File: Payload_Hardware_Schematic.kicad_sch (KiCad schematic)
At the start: 8 parts, among them J1 Micro_SD_Card, J2 Conn_01x02_Socket, J4 Conn_01x02, U1 STM32F411 BlackPill, U2 MPM3610, U4 LSM9DS1, U5 MPM3610, U6 BMP388

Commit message: servo pins
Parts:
- added J3, J5: Conn_01x04_Pin, Connector_PinHeader_2.54mm:PinHeader_1x04_P2.54mm_Vertical, symbol Connector:Conn_01x04_Pin
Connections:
- net 5V: now also J3.3 (Pin_3), J5.3 (Pin_3)
- net FDBK1: now also J3.1 (Pin_1)
- net GND: now also J3.4 (Pin_4), J5.4 (Pin_4)
- net TIM1: now also J3.2 (Pin_2)
- net TIM2: now also J5.2 (Pin_2)
- net FDBK renamed FDBK2
- net FDBK2: now also J5.1 (Pin_1)
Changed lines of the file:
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@@
+		)
+	)
+	(label "GND"
+		(at 121.92 100.33 0)
+		(effects
+			(font
+				(size 1.27 1.27)
+				(thickness 0.254)
+				(bold yes)
+			)
+			(justify left bottom)
 		)
 	)
@@
 		)
 	)
+	(label "5V"
+		(at 140.97 97.79 0)
+		(effects
+			(font
+				(size 1.27 1.27)
+				(thickness 0.254)
+				(bold yes)
+				(color 255 0 0 1)
+			)
+			(justify left bottom)
+		)
+	)
+	(label "5V"
+		(at 121.92 97.79 0)
+		(effects
+			(font
+				(size 1.27 1.27)
+				(thickness 0.254)
+				(bold yes)
+				(color 255 0 0 1)
+			)
+			(justify left bottom)
+		)
+	)
 	(label "MISO4"
 		(at 29.21 39.37 180)
@@
 				(thickness 0.254)
 				(bold yes)
-				(color 23 39 255 1)
+				(color 70 255 55 1)
 			)
 			(justify left bottom)
@@
 		)
 	)
-	(label "FDBK"
+	(label "FDBK2"
 		(at 242.57 34.29 0)
 		(effects
@@
 				(thickness 0.254)
 				(bold yes)
-				(color 164 74 255 1)
+				(color 0 255 0 1)
 			)
 			(justify left bottom)
@@
 		)
 	)
+	(label "GND"
+		(at 140.97 100.33 0)
+		(effects
+			(font
+				(size 1.27 1.27)
+				(thickness 0.254)
+				(bold yes)
+			)
+			(justify left bottom)
+		)
+	)
 	(label "SCK3"
 		(at 157.48 38.1 0)
@@
 		)
 	)
+	(label "FDBK2"
+		(at 121.92 92.71 0)
+		(effects
+			(font
+				(size 1.27 1.27)
+				(thickness 0.254)
+				(bold yes)
+				(color 0 255 0 1)
+			)
+			(justify left bottom)
+		)
+	)
 	(label "MISO3"
 		(at 157.48 35.56 0)
@@
 		)
 	)
+	(label "TIM2"
+		(at 121.92 95.25 0)
+		(effects
+			(font
+				(size 1.27 1.27)
+			)
+			(justify left bottom)
+		)
+	)
 	(label "SCK2"
 		(at 83.82 36.83 180)
@@
 		)
 	)
+	(label "FDBK1"
+		(at 140.97 92.71 0)
+		(effects
+			(font
+				(size 1.27 1.27)
+				(thickness 0.254)
+				(bold yes)
+				(color 70 255 55 1)
+			)
+			(justify left bottom)
+		)
+	)
 	(label "MOSI4"
 		(at 186.69 41.91 180)
@@
 				(bold yes)
 				(color 23 39 255 1)
+			)
+			(justify left bottom)
+		)
+	)
+	(label "TIM1"
+		(at 140.97 95.25 0)
+		(effects
+			(font
+				(size 1.27 1.27)
 			)
 			(justify left bottom)
@@
 		(on_board yes)
 		(dnp no)
-		(fields_autoplaced yes)
 		(property "Reference" "U5"
 			(at 148.59 67.31 0)
@@
 	)
 	(symbol
+		(lib_id "Connector:Conn_01x04_Pin")
+		(at 135.89 95.25 0)
+		(unit 1)
+		(exclude_from_sim no)
+		(in_bom yes)
+		(on_board yes)
+		(dnp no)
+		(fields_autoplaced yes)
+		(property "Reference" "J3"
+			(at 136.525 87.63 0)
+			(effects
+				(font
+					(size 1.27 1.27)
+				)
+			)
+		)
+		(property "Value" "Conn_01x04_Pin"
+			(at 136.525 90.17 0)
+			(effects
+				(font
+					(size 1.27 1.27)
+				)
+			)
+		)
+		(property "Footprint" "Connector_PinHeader_2.54mm:PinHeader_1x04_P2.54mm_Vertical"
+			(at 135.89 95.25 0)
+			(effects
+				(font
+					(size 1.27 1.27)
+				)
+				(hide yes)
+			)
+		)
+		(property "Datasheet" "~"
+			(at 135.89 95.25 0)
+			(effects
+				(font
+					(size 1.27 1.27)
+				)
+				(hide yes)
+			)
+		)
+		(property "Description" "Generic connector, single row, 01x04, script generated"
+			(at 135.89 95.25 0)
+			(effects
+				(font
+					(size 1.27 1.27)
+				)
+				(hide yes)
+			)
+		)
+		(pin "2"
+		)
+		(pin "1"
+		)
+		(pin "4"
+		)
+		(pin "3"
+		)
+		(instances
+			(project ""
+				(path "/f4ead8bb-2437-4e54-a6d9-f5ca11bfd675"
+					(reference "J3")
+					(unit 1)
+				)
+			)
+		)
+	)
+	(symbol
 		(lib_id "Payload-STM32:STM32F411_Black_Pill")
 		(at 214.63 53.34 0)
@@
 					(unit 1)
 				)
+			)
+		)
+	)
+	(symbol
+		(lib_id "Connector:Conn_01x04_Pin")
+		(at 116.84 95.25 0)
+		(unit 1)
+		(exclude_from_sim no)
+		(in_bom yes)
+		(on_board yes)
+		(dnp no)
+		(property "Reference" "J5"
+			(at 117.475 87.63 0)
+			(effects
+				(font
+					(size 1.27 1.27)
+				)
+			)
+		)
+		(property "Value" "Conn_01x04_Pin"
+			(at 117.475 90.17 0)
+			(effects
+				(font
+					(size 1.27 1.27)
+				)
+			)
+		)
+		(property "Footprint" "Connector_PinHeader_2.54mm:PinHeader_1x04_P2.54mm_Vertical"
+			(at 116.84 95.25 0)
+			(effects
+				(font
+					(size 1.27 1.27)
+				)
+				(hide yes)
+			)
+		)
+		(property "Datasheet" "~"
+			(at 116.84 95.25 0)
+			(effects
+				(font
+					(size 1.27 1.27)
+				)
+				(hide yes)
+			)
+		)
+		(property "Description" "Generic connector, single row, 01x04, script generated"
+			(at 116.84 95.25 0)
+			(effects
+				(font
+					(size 1.27 1.27)
+				)
+				(hide yes)
+			)
+		)
+		(pin "2"
+		)
+		(pin "1"
+		)
+		(pin "4"
+		)
+		(pin "3"
+		)
+		(instances
+			(project "Payload_Hardware_Schematic"
+				(path "/f4ead8bb-2437-4e54-a6d9-f5ca11bfd675"
+					(reference "J5")
+					(unit 1)
+				)

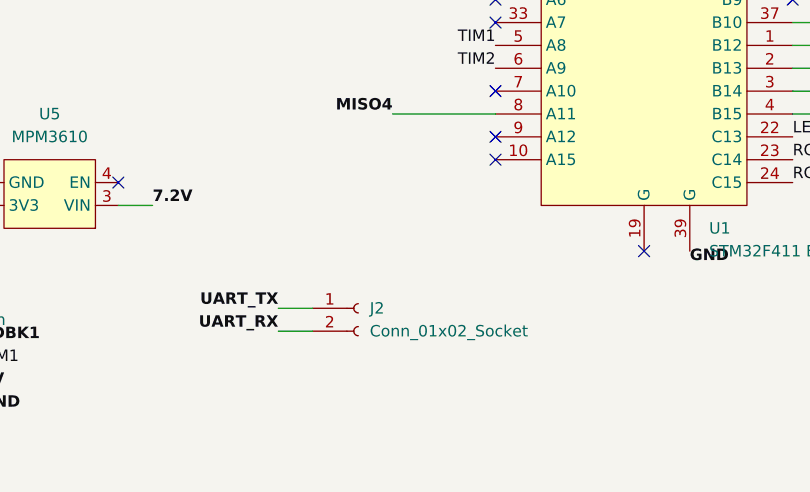
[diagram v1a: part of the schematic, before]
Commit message: added DIO SCK
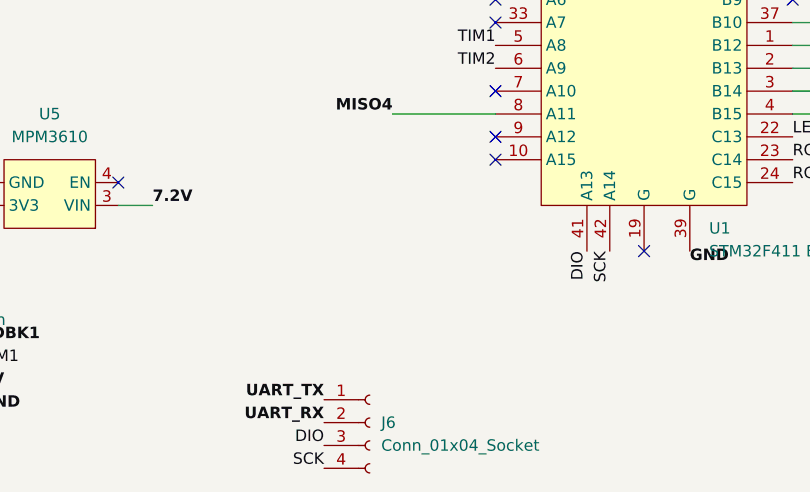
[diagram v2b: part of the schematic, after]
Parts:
- removed J2: Conn_01x02_Socket, Connector_PinSocket_2.54mm:PinSocket_1x02_P2.54mm_Vertical, symbol Connector:Conn_01x02_Socket
- added J6: Conn_01x04_Socket, symbol Connector:Conn_01x04_Socket
- U1: footprint Avionics_Symbols:STM32F411 -> Payload-STM32:STM32F411_Black_Pill
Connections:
- net UART_RX: now also J6.2 (Pin_2)
- net UART_TX: now also J6.1 (Pin_1)
- new net DIO: J6.3 (Pin_3), U1.41 (A13)
- new net SCK: J6.4 (Pin_4), U1.42 (A14)
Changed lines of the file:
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@@
-	(wire
-		(pts
-			(xy 173.99 88.9) (xy 177.8 88.9)
-		)
-		(stroke
-			(width 0)
-			(type default)
-		)
-	)
 	(wire
 		(pts
@@
 		(pts
 			(xy 83.82 41.91) (xy 88.9 41.91)
-		)
-		(stroke
-			(width 0)
-			(type default)
-		)
-	)
-	(wire
-		(pts
-			(xy 173.99 91.44) (xy 177.8 91.44)
 		)
 		(stroke
@@
 		)
 	)
+	(label "DIO"
+		(at 208.28 82.55 270)
+		(effects
+			(font
+				(size 1.27 1.27)
+			)
+			(justify right bottom)
+		)
+	)
 	(label "CSIMU"
 		(at 231.14 46.99 0)
@@
 		)
 	)
+	(label "SCK"
+		(at 210.82 82.55 270)
+		(effects
+			(font
+				(size 1.27 1.27)
+			)
+			(justify right bottom)
+		)
+	)
 	(label "GND"
 		(at 140.97 100.33 0)
@@
 		)
 	)
+	(label "UART_RX"
+		(at 179.07 101.6 180)
+		(effects
+			(font
+				(size 1.27 1.27)
+				(thickness 0.254)
+				(bold yes)
+				(color 221 133 0 1)
+			)
+			(justify right bottom)
+		)
+	)
 	(label "3.3V"
 		(at 215.9 20.32 0)
@@
 		)
 	)
+	(label "SCK"
+		(at 179.07 106.68 180)
+		(effects
+			(font
+				(size 1.27 1.27)
+			)
+			(justify right bottom)
+		)
+	)
 	(label "RCC_OSC32_OUT"
 		(at 231.14 74.93 0)
@@
 		)
 	)
+	(label "DIO"
+		(at 179.07 104.14 180)
+		(effects
+			(font
+				(size 1.27 1.27)
+			)
+			(justify right bottom)
+		)
+	)
 	(label "GND"
 		(at 58.42 74.93 180)
@@
 		)
 	)
-	(label "UART_RX"
-		(at 173.99 91.44 180)
-		(effects
-			(font
-				(size 1.27 1.27)
-				(thickness 0.254)
-				(bold yes)
-				(color 221 133 0 1)
-			)
-			(justify right bottom)
-		)
-	)
 	(label "BTN"
 		(at 198.12 39.37 180)
@@
 	)
 	(label "UART_TX"
-		(at 173.99 88.9 180)
+		(at 179.07 99.06 180)
 		(effects
 			(font
@@
 	)
 	(symbol
+		(lib_id "Connector:Conn_01x04_Socket")
+		(at 184.15 101.6 0)
+		(unit 1)
+		(exclude_from_sim no)
+		(in_bom yes)
+		(on_board yes)
+		(dnp no)
+		(fields_autoplaced yes)
+		(property "Reference" "J6"
+			(at 185.42 101.5999 0)
+			(effects
+				(font
+					(size 1.27 1.27)
+				)
+				(justify left)
+			)
+		)
+		(property "Value" "Conn_01x04_Socket"
+			(at 185.42 104.1399 0)
+			(effects
+				(font
+					(size 1.27 1.27)
+				)
+				(justify left)
+			)
+		)
+		(property "Footprint" ""
+			(at 184.15 101.6 0)
+			(effects
+				(font
+					(size 1.27 1.27)
+				)
+				(hide yes)
+			)
+		)
+		(property "Datasheet" "~"
+			(at 184.15 101.6 0)
+			(effects
+				(font
+					(size 1.27 1.27)
+				)
+				(hide yes)
+			)
+		)
+		(property "Description" "Generic connector, single row, 01x04, script generated"
+			(at 184.15 101.6 0)
+			(effects
+				(font
+					(size 1.27 1.27)
+				)
+				(hide yes)
+			)
+		)
+		(pin "4"
+		)
+		(pin "2"
+		)
+		(pin "1"
+		)
+		(pin "3"
+		)
+		(instances
+			(project ""
+				(path "/f4ead8bb-2437-4e54-a6d9-f5ca11bfd675"
+					(reference "J6")
+					(unit 1)
+				)
+			)
+		)
+	)
+	(symbol
 		(lib_id "Connector:Conn_01x04_Pin")
 		(at 135.89 95.25 0)
@@
 			)
 		)
-		(property "Footprint" "Avionics_Symbols:STM32F411"
+		(property "Footprint" "Payload-STM32:STM32F411_Black_Pill"
 			(at 210.82 39.37 0)
 			(effects
@@
 		)
 		(pin "24"
+		)
+		(pin "42"
+		)
+		(pin "41"
 		)
 		(instances
@@
 					(unit 1)
 				)
-			)
-		)
-	)
-	(symbol
-		(lib_id "Connector:Conn_01x02_Socket")
-		(at 182.88 88.9 0)
-		(unit 1)
-		(exclude_from_sim no)
-		(in_bom yes)
-		(on_board yes)
-		(dnp no)
-		(fields_autoplaced yes)
-		(property "Reference" "J2"
-			(at 184.15 88.8999 0)
-			(effects
-				(font
-					(size 1.27 1.27)
-				)
-				(justify left)
-			)
-		)
-		(property "Value" "Conn_01x02_Socket"
-			(at 184.15 91.4399 0)
-			(effects
-				(font
-					(size 1.27 1.27)
-				)
-				(justify left)
-			)
-		)
-		(property "Footprint" "Connector_PinSocket_2.54mm:PinSocket_1x02_P2.54mm_Vertical"
-			(at 182.88 88.9 0)
-			(effects
-				(font
-					(size 1.27 1.27)
-				)
-				(hide yes)
-			)
-		)
-		(property "Datasheet" "~"
-			(at 182.88 88.9 0)
-			(effects
-				(font
-					(size 1.27 1.27)
-				)
-				(hide yes)
-			)
-		)
-		(property "Description" "Generic connector, single row, 01x02, script generated"
-			(at 182.88 88.9 0)
-			(effects
-				(font
-					(size 1.27 1.27)
-				)
-				(hide yes)
-			)
-		)
-		(pin "2"
-		)
-		(pin "1"
-		)
-		(instances
-			(project ""
-				(path "/f4ead8bb-2437-4e54-a6d9-f5ca11bfd675"
-					(reference "J2")
-					(unit 1)
-				)

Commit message: auto wiring
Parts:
- added H1, H2, H3, H4: MountingHole, MountingHole:MountingHole_3.2mm_M3_DIN965_Pad, symbol Mechanical:MountingHole
- J3, J5: footprint Connector_PinHeader_2.54mm:PinHeader_1x04_P2.54mm_Vertical -> Connector_PinHeader_2.54mm:PinHeader_1x04_P2.54mm_Horizontal
- J6: footprint (none) -> Connector_PinHeader_2.54mm:PinHeader_1x04_P2.54mm_Horizontal

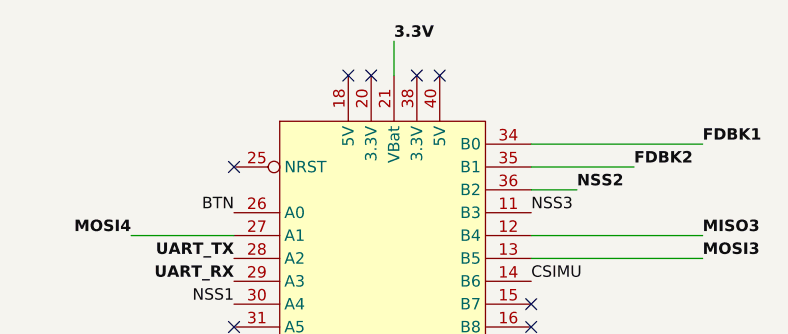
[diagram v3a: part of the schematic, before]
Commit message: finalized board, changed Vbat to 3.3V
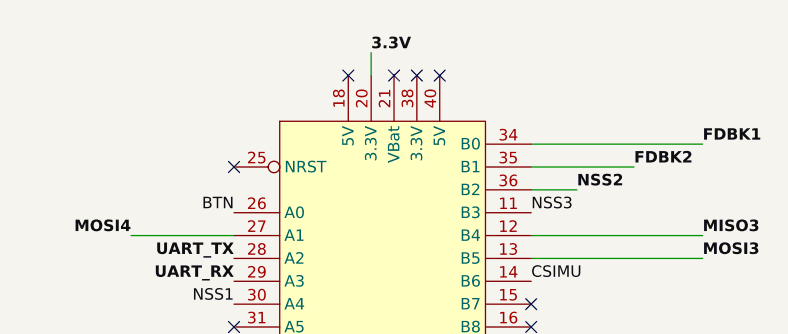
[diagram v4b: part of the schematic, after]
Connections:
- net at J1.1 (3V), U4.1 (VIN), U5.2 (3V3)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: now also U1.20 (3.3V); no longer U1.21 (VBat)
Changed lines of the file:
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@@
-	)
-	(no_connect
-		(at 213.36 24.13)
 	)
 	(no_connect
@@
 	)
 	(no_connect
+		(at 215.9 24.13)
+	)
+	(no_connect
 		(at 157.48 27.94)
 	)
@@
 	(wire
 		(pts
-			(xy 215.9 20.32) (xy 215.9 24.13)
-		)
-		(stroke
-			(width 0)
-			(type default)
-		)
-	)
-	(wire
-		(pts
 			(xy 186.69 41.91) (xy 198.12 41.91)
 		)
@@
 		(pts
 			(xy 83.82 41.91) (xy 88.9 41.91)
+		)
+		(stroke
+			(width 0)
+			(type default)
+		)
+	)
+	(wire
+		(pts
+			(xy 213.36 21.59) (xy 213.36 24.13)
 		)
 		(stroke
@@
 		)
 	)
-	(label "3.3V"
-		(at 215.9 20.32 0)
-		(effects
-			(font
-				(size 1.27 1.27)
-				(thickness 0.254)
-				(bold yes)
-				(color 255 0 0 1)
-			)
-			(justify bottom)
-		)
-	)
 	(label "GND"
 		(at 113.03 41.91 0)
@@
 		)
 	)
+	(label "3.3V"
+		(at 213.36 21.59 0)
+		(effects
+			(font
+				(size 1.27 1.27)
+				(thickness 0.254)
+				(bold yes)
+				(color 255 0 0 1)
+			)
+			(justify bottom)
+		)
+	)

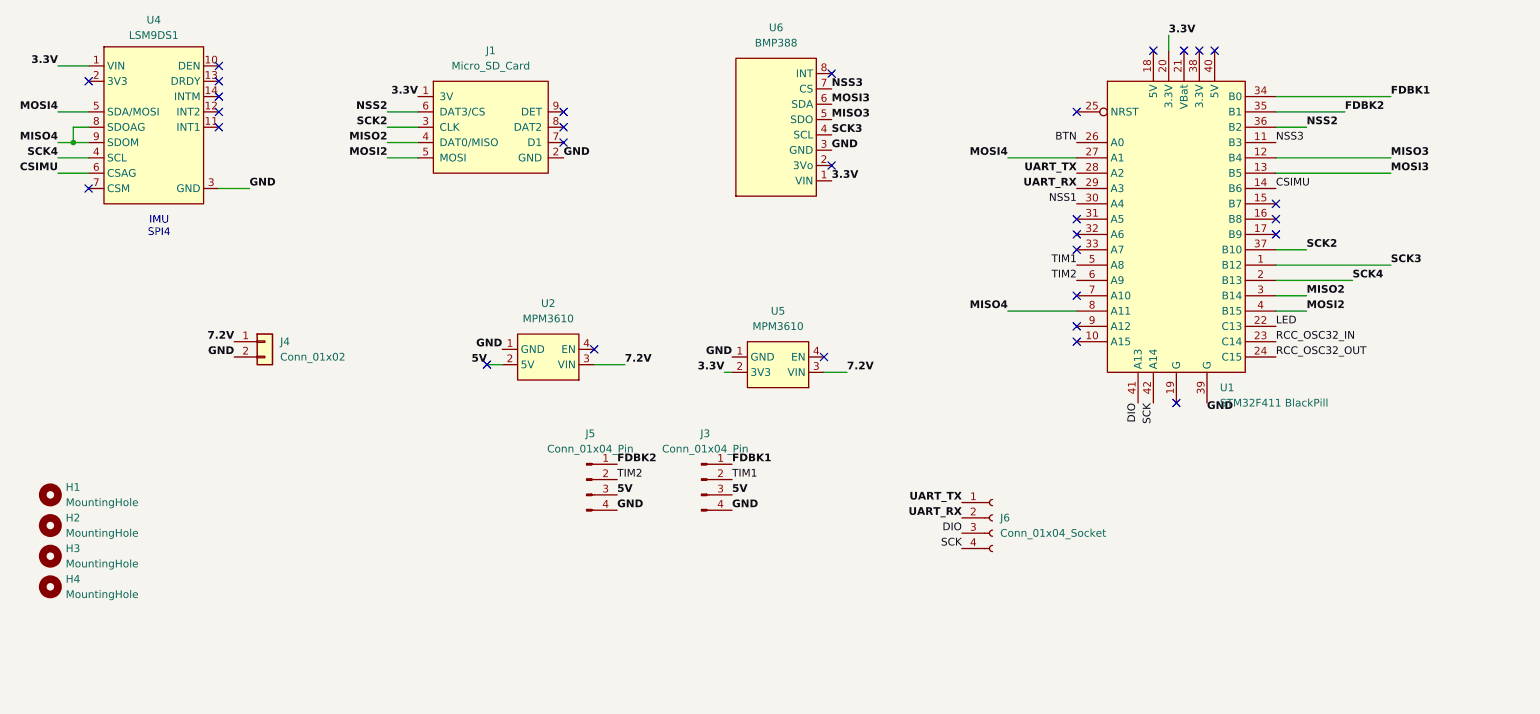
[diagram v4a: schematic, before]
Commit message: Niv's edits, moved pins close to edge and connected servos to 7.2V
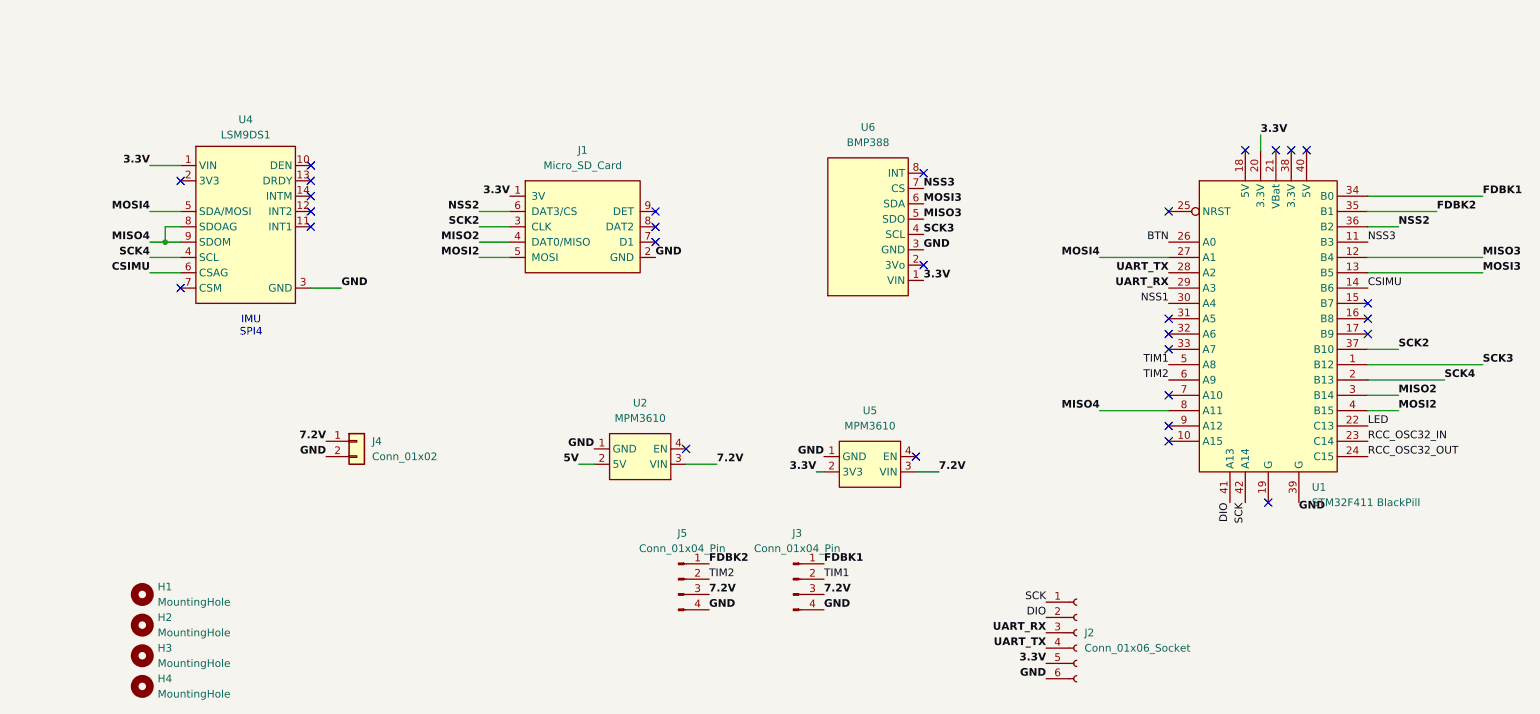
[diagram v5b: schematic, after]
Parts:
- removed J6: Conn_01x04_Socket, Connector_PinHeader_2.54mm:PinHeader_1x04_P2.54mm_Horizontal, symbol Connector:Conn_01x04_Socket
- added J2: Conn_01x06_Socket, Connector_PinSocket_2.54mm:PinSocket_1x06_P2.54mm_Horizontal, symbol Connector:Conn_01x06_Socket
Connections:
- net 5V: no longer J3.3 (Pin_3), J5.3 (Pin_3)
- net 7.2V: now also J3.3 (Pin_3), J5.3 (Pin_3)
- net DIO: now also J2.2 (Pin_2)
- net GND: now also J2.6 (Pin_6)
- net SCK: now also J2.1 (Pin_1)
- net UART_RX: now also J2.3 (Pin_3)
- net UART_TX: now also J2.4 (Pin_4)
- net at J1.1 (3V), U1.20 (3.3V), U4.1 (VIN)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: now also J2.5 (Pin_5)
- no-connect marks 30 -> 29
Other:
- moved on the sheet: H1, H2, H3, H4, J1, J3, J4, J5, U1, U2, U4, U5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
